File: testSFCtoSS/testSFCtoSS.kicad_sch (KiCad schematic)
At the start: 13 parts, among them J1 SFC Controler, J2 SegaSaturn Controler, U1 4024, U2 NE555D, U3 74LS21, U4 74LS32, U5 HEF4094B, U6 HEF4094B, U7 74LS153, U8 74LS153

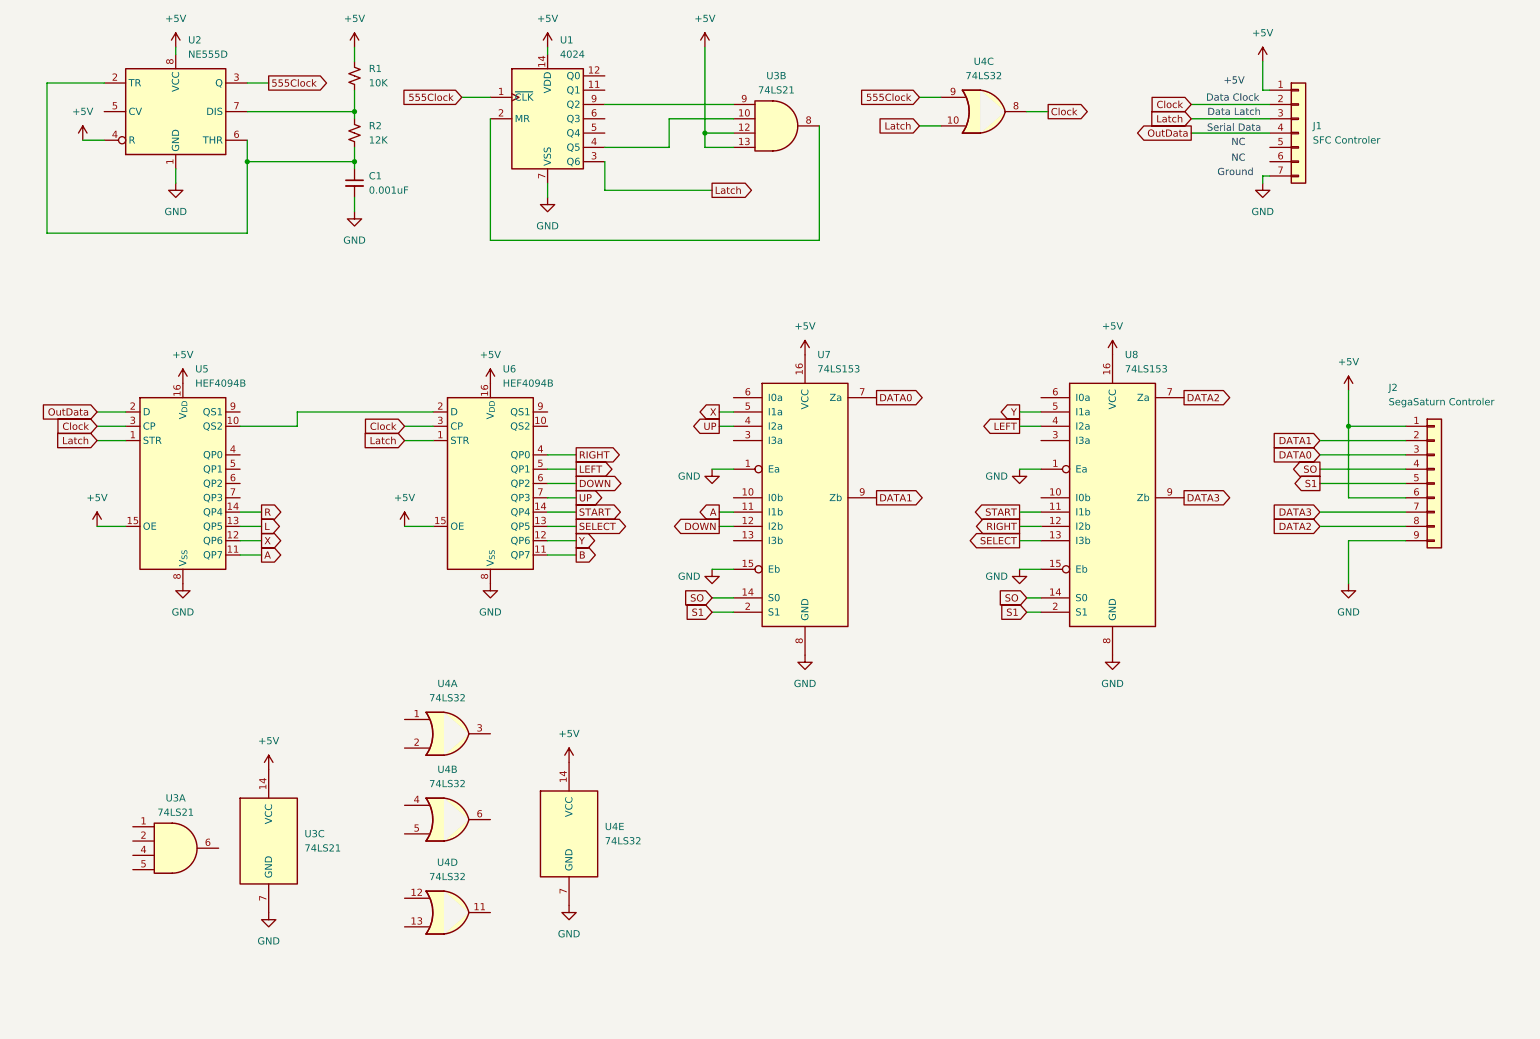
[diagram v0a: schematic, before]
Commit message: SFC Controller Serial->Parallel
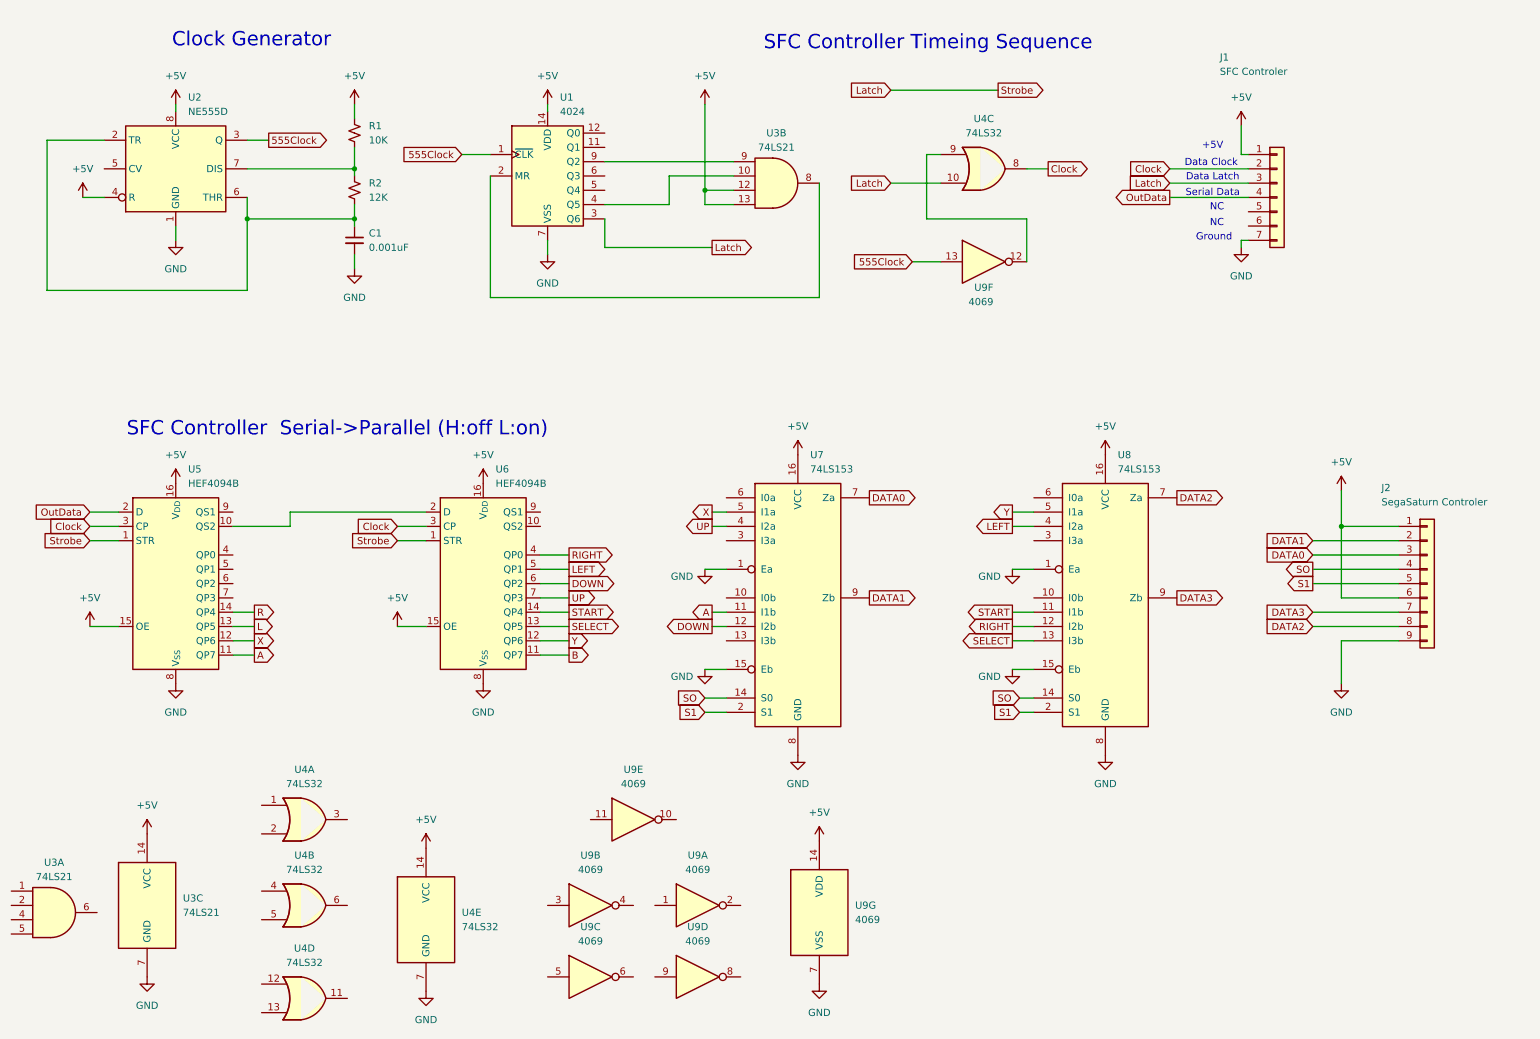
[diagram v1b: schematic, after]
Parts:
- added U9: 4069, symbol 4xxx:4069
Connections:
- net +5V: now also U9.14 (VDD)
- net 555Clock: now also U9.13; no longer U4.9
- net GND: now also U9.7 (VSS)
- new net: U4.9, U9.12
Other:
- note added: "Clock Generator"
- note added: "SFC Controller Serial->Parallel (H:off L:on)"
- note added: "SFC Controller Timeing Sequence"
- moved on the sheet: C1, J1, J2, R1, R2, U1, U2, U3A, U3B, U3C, U4A, U4B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

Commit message: convert NAND
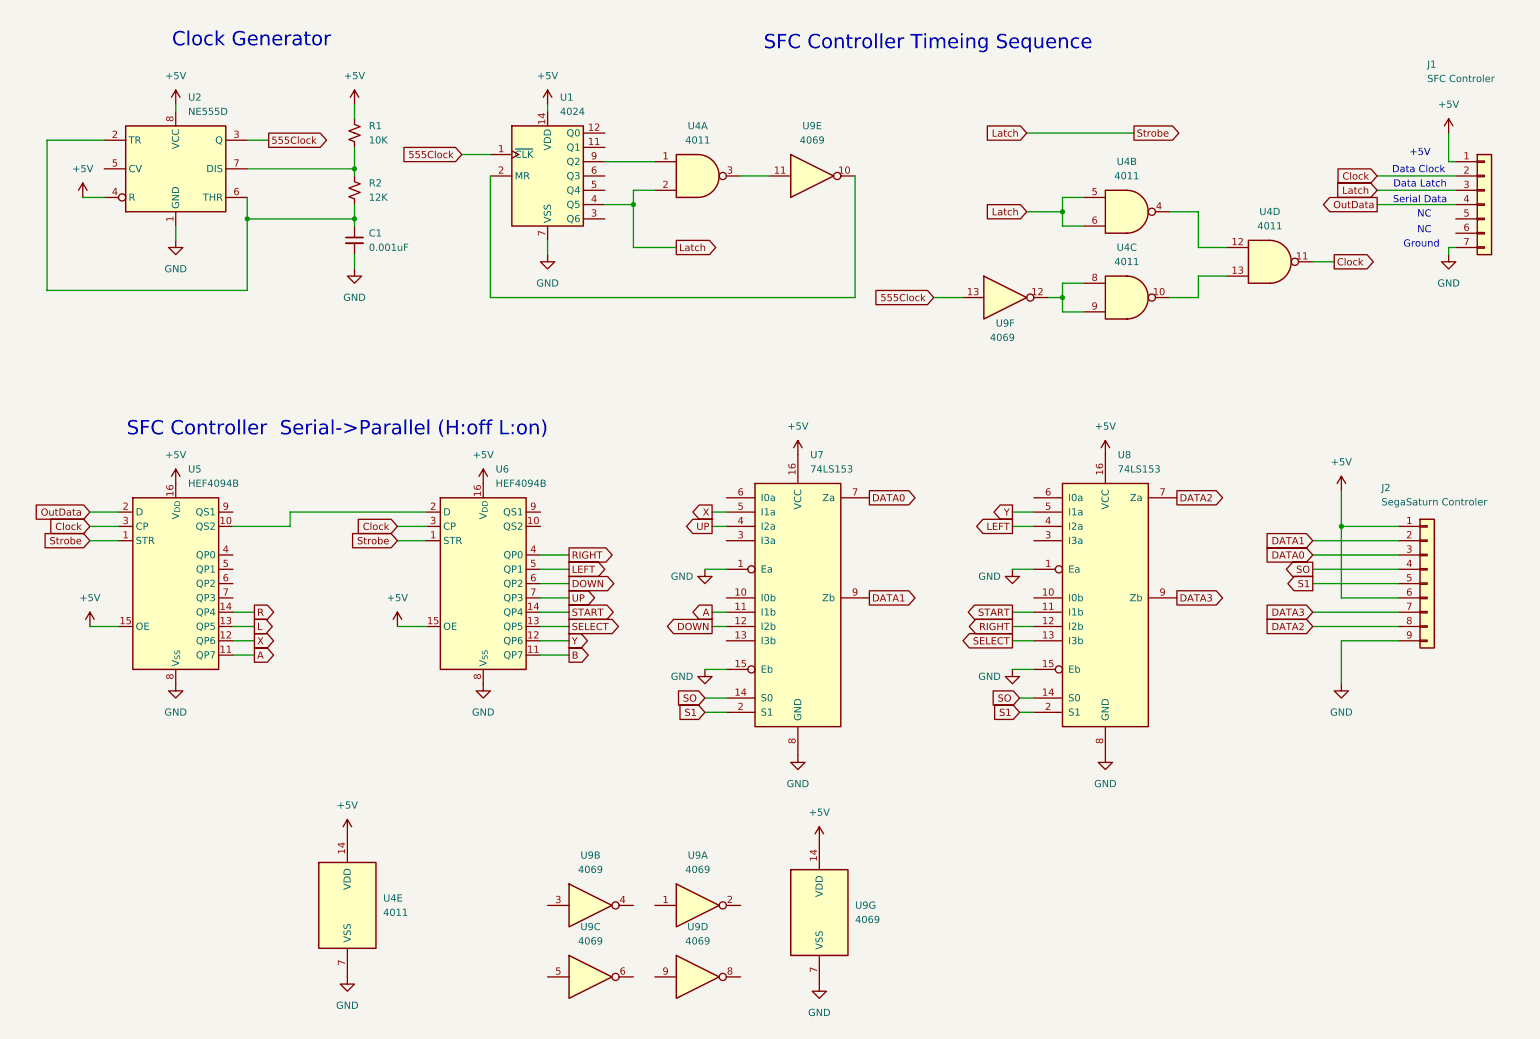
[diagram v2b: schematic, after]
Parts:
- removed U3: 74LS21, symbol 74xx:74LS21
- removed U4: 74LS32, symbol 74xx:74LS32
- added U4: 4011, symbol 4xxx:4011
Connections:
- net +5V: now also U4.14 (VDD)
- net Clock: now also U4.11
- net GND: now also U4.7 (VSS)
- net Latch: now also U1.4 (Q5), U4.2, U4.5, U4.6; no longer U1.3 (Q6)
- net at U1.2 (MR): now also U9.10
- net at U1.9 (Q2): now also U4.1
- net at U9.11: now also U4.3
- net at U9.12: now also U4.8, U4.9
- new net: U4.12, U4.4
- new net: U4.10, U4.13
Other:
- moved on the sheet: J1, U9E, U9F

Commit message: debug
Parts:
- removed unit 3 of U9
- C1: value 0.001uF -> 470pF
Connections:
- net Latch: now also U1.5 (Q4); no longer U1.4 (Q5)
- net at U4.1: now also U1.12 (Q0); no longer U1.9 (Q2)
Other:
- moved on the sheet: U4B, U4C, U4D, U9F

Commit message: update
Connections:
- net +5V: now also U7.10 (I0b), U7.13 (I3b), U7.3 (I3a), U7.6 (I0a), U8.10 (I0b), U8.3 (I3a), U8.6 (I0a)
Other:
- note added: "A"
- note added: "B"
- note added: "C"
- note added: "Dn"
- note added: "L"
- note added: "Lt"
- note added: "R"
- note added: "Rt"
- note added: "St"
- note added: "Up"
- note added: "X"
- note added: "Y"
- note added: "Z"
- note added: "nc"
- moved on the sheet: U7, U8
